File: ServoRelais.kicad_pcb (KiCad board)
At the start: 2 copper layers, 38.7 x 24.9 mm, 20 parts, among them J1 Conn_01x03_Female, J2 ISCP, J3 Conn_01x02_Female, J4 Conn_01x03_Female, U1 L78L05_SOT89, U2 PIC10F320-IP, U3 ASSR-1611

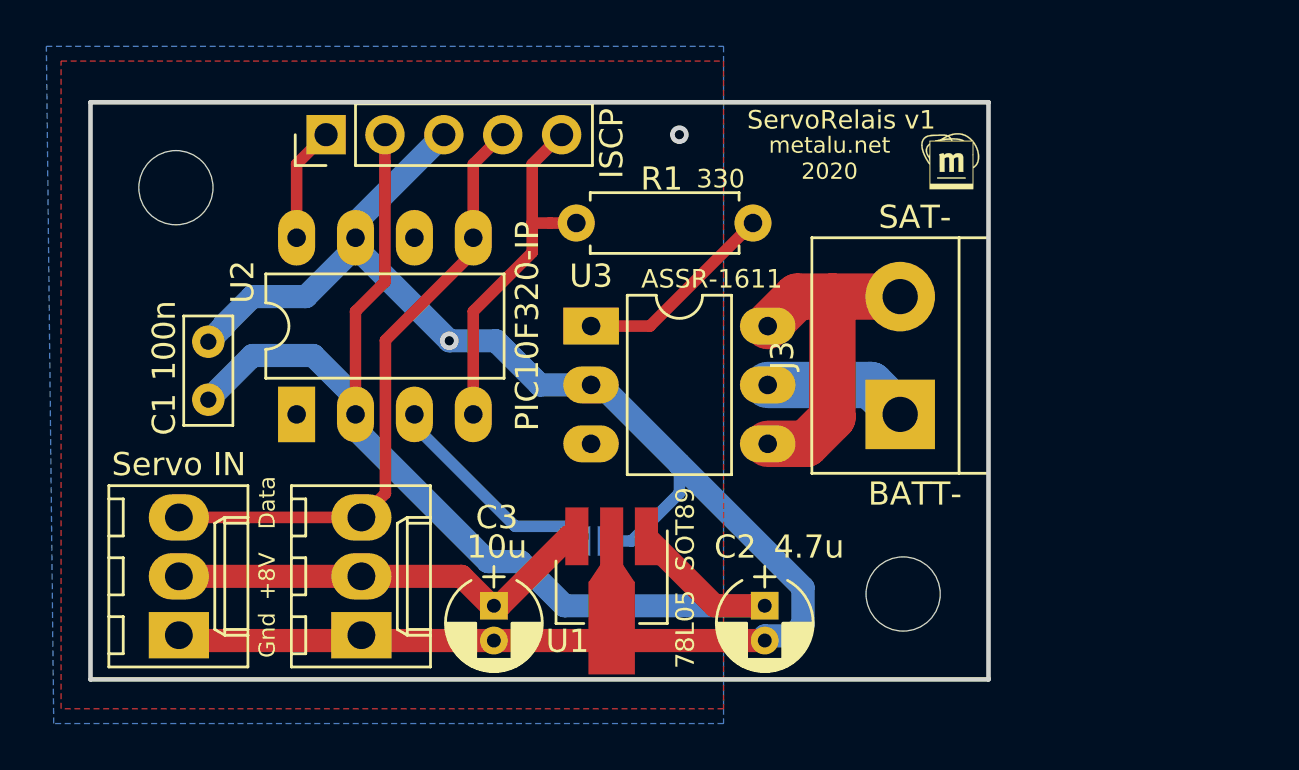
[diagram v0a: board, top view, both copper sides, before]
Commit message: finish PCB, using ASSR-1611 as a 5A circuit breaker.
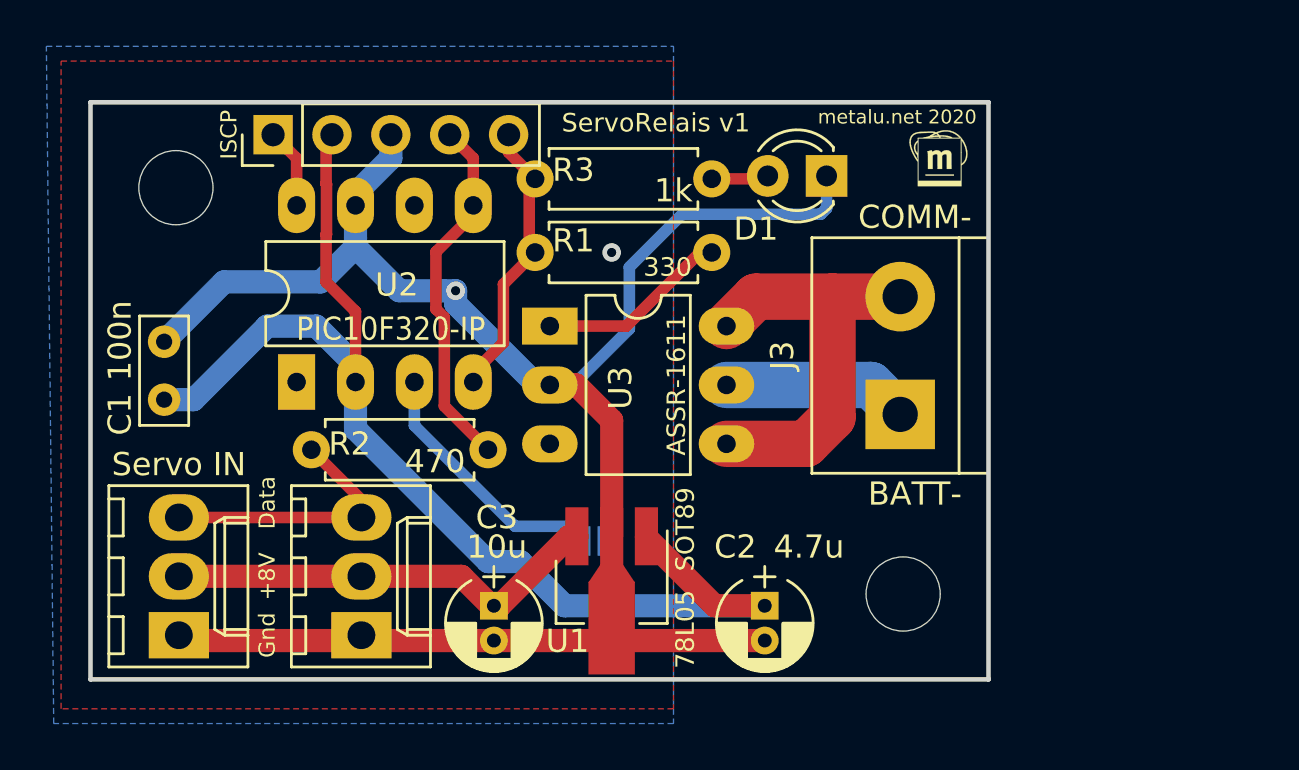
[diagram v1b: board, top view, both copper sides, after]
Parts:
- added D1: LED, LEDs:LED_D3.0mm, F.Cu at (88.4, 33.5)
- added R2: 470, Resistors_ThroughHole:R_Axial_DIN0207_L6.3mm_D2.5mm_P7.62mm_Horizontal, F.Cu at (73.8, 45.3)
- added R3: 1k, Resistors_ThroughHole:R_Axial_DIN0207_L6.3mm_D2.5mm_P7.62mm_Horizontal, F.Cu at (83.4, 33.7)
- moved G*** 15.8 mm to (86.1, 48.1)
- moved J2 2.29 mm to (64.5, 31.8)
- moved R1 2.18 mm to (83.4, 36.8)
- moved C1 1.91 mm to (59.8, 43.2)
- moved U3 1.78 mm to (76.5, 40.0)
- moved U2 1.40 mm to (65.5, 42.4)
- moved G*** 0.52 mm to (93.2, 32.8)
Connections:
- J1 pad 3: /PGD -> Net-(J1-Pad3)
- J4 pad 3: /PGD -> Net-(J1-Pad3)
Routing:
- net Net-(J1-Pad3): track 0.00 -> 11.7 mm
- net /PGD: track 26.9 -> 15.6 mm
- net GND: track 78.5 -> 82.7 mm
- net Net-(J3-Pad2): track 14.7 -> 18.3 mm
- net /PGC: track 15.5 -> 12.0 mm
- net +5V: track 49.0 -> 51.5 mm
- net Net-(D1-Pad2): track 0.00 -> 2.47 mm
- net Net-(J3-Pad1): track 6.24 -> 8.02 mm
- net /Vpp: track 4.97 -> 3.47 mm
- net Net-(JP1-Pad1): track 9.42 -> 10.8 mm
- net Net-(R1-Pad1): track 8.83 -> 8.30 mm
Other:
- board text added: "COMM-"
- board text removed: "SAT-"

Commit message: use a 3v->9V dc-dc converter. version 1.3
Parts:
- removed U3: ASSR-1611, Housings_DIP:DIP-6_W7.62mm_LongPads
- added Q1: IRLB8721PBF, TO_SOT_Packages_SMD:TO-252-2, F.Cu at (83.3, 42.9)
- added Q2: IRLB8721PBF, TO_SOT_Packages_SMD:TO-252-2, F.Cu at (95.1, 45.7)
- added R4: 1k, Resistors_ThroughHole:R_Axial_DIN0207_L6.3mm_D2.5mm_P7.62mm_Horizontal, F.Cu at (97.0, 53.7)
- C3: value 10u -> 100n; footprint Capacitors_ThroughHole:CP_Radial_D4.0mm_P1.50mm -> Capacitors_ThroughHole:C_Rect_L4.6mm_W2.0mm_P2.50mm_MKS02_FKP02
- R1: value 330 -> 1k
- R3: value 1k -> 2.2k
- U1: value L78L05_SOT89 -> MEE1-0309; footprint TO_SOT_Packages_SMD:SOT-89-3_Handsoldering -> Converters_DCDC_ACDC:DCDC-Conv_muRata_CRE1xxxxxxSC
- moved C3 26.3 mm to (94.9, 35.9), turned to 90 degrees
- moved G*** 22.6 mm to (82.0, 52.5)
- moved R3 22.1 mm to (97.0, 51.1)
- moved D1 19.8 mm to (104.5, 45.0), turned to 270 degrees
- moved U1 15.6 mm to (81.9, 35.7), turned to 90 degrees
- moved J3 11.6 mm to (102.4, 39.6)
- moved C2 11.6 mm to (74.2, 52.1)
- moved H2 11.4 mm to (103.1, 51.8)
- moved R1 8.92 mm to (76.2, 42.0), turned to 90 degrees
- moved G*** 5.82 mm to (89.5, 43.4)
- moved C1 3.25 mm to (62.6, 41.5)
- moved JP1 1.35 mm to (79.4, 50.2)
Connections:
- C1 pad 1: +5V -> +3V3
- C2 pad 1: +5V -> +3V3
- C3 pad 1: VCC -> Net-(C3-Pad1)
- C3 pad 2: GND -> GNDPWR
- D1 pad 1: GND -> GNDPWR
- J1 pad 2: VCC -> +3V3
- J2 pad 2: +5V -> +3V3
- J3 pad 1: Net-(J3-Pad1) -> GNDPWR
- J4 pad 2: VCC -> +3V3
- R1 pad 1: Net-(R1-Pad1) -> GND
- R3 pad 2: /PGC -> Net-(C3-Pad1)
- U1 pad 1: +5V -> Net-(Q1-Pad2)
- U1 pad 2: GND -> +3V3
- U1 pad 3: VCC -> GNDPWR
- U2 pad 2: +5V -> +3V3
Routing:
- net +3V3: track 0.00 -> 65.4 mm
- net GNDPWR: track 0.00 -> 58.4 mm
- net +5V: track 51.5 -> 0.00 mm
- net GND: track 82.7 -> 39.8 mm, vias 2 -> 0
- net Net-(C3-Pad1): track 0.00 -> 36.4 mm
- net VCC: track 18.9 -> 0.00 mm
- net Net-(Q1-Pad2): track 0.00 -> 8.69 mm
- net Net-(R1-Pad1): track 8.30 -> 0.00 mm
- net Net-(J3-Pad1): track 8.02 -> 0.00 mm
- net Net-(D1-Pad2): track 2.47 -> 8.97 mm
- net /PGC: track 12.0 -> 17.6 mm
- net Net-(J3-Pad2): track 18.3 -> 13.4 mm
- net Net-(JP1-Pad1): track 10.8 -> 12.4 mm
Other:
- board size 38.7 x 24.9 mm -> 49.9 x 24.9 mm
- board text removed: "78L05"
- board text removed: "SOT89"

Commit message: PCB: add solder-switch to disable powering the DC-DC converter (else programming of the PIC fails because of power loss)
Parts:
- added JP2: (prog), Connect:GS2, B.Cu at (83.1, 39.0)
- moved G*** 3.19 mm to (92.7, 43.2)
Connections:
- U1 pad 2: +3V3 -> Net-(JP2-Pad2)
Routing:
- net Net-(JP2-Pad2): track 0.00 -> 3.62 mm
- net +3V3: track 65.4 -> 61.9 mm
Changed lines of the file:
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@@
     (thickness 1.6)
     (drawings 15)
-    (tracks 98)
+    (tracks 100)
     (zones 0)
-    (modules 25)
-    (nets 13)
+    (modules 26)
+    (nets 14)
   )
   (page User 159.995 110.007)
@@
   (net 11 +3V3)
   (net 12 "Net-(C3-Pad1)")
+  (net 13 "Net-(JP2-Pad2)")
   (net_class Default "This is the default net class."
     (clearance 0.2)
@@
     (add_net "Net-(J3-Pad2)")
     (add_net "Net-(JP1-Pad1)")
+    (add_net "Net-(JP2-Pad2)")
     (add_net "Net-(Q1-Pad2)")
   )
@@
   )
   (module metalunet:metalunet (layer B.Cu)
-    (at 89.535 43.434 180)
+    (at 92.71 43.18 180)
     (fp_text reference G*** (at 3.81 1.143 180) (layer B.SilkS) hide
       (effects (font (size 0.3 0.3) (thickness 0.075)) (justify mirror))
@@
       (net 10 "Net-(Q1-Pad2)"))
     (pad 2 thru_hole oval (at 0 2.54) (size 1.5 2) (drill 0.7) (layers *.Cu *.Mask)
-      (net 11 +3V3))
+      (net 13 "Net-(JP2-Pad2)"))
     (pad 3 thru_hole oval (at 0 5.08) (size 1.5 2) (drill 0.7) (layers *.Cu *.Mask)
       (net 9 GNDPWR))
@@
     )
   )
+  (module Connect:GS2 (layer B.Cu)
+    (at 83.058 38.989 270)
+    (descr "2-pin solder bridge")
+    (tags "solder bridge")
+    (attr smd)
+    (fp_text reference JP2 (at 1.78 0 180) (layer B.SilkS) hide
+      (effects (font (size 1 1) (thickness 0.15)) (justify mirror))
+    )
+    (fp_text value "(prog)" (at 1.524 0 180) (layer B.SilkS)
+      (effects (font (size 0.7 0.7) (thickness 0.1)) (justify mirror))
+    )
+    (fp_line (start -0.89 1.27) (end 0.89 1.27) (layer B.SilkS) (width 0.12))
+    (fp_line (start 0.89 -1.27) (end -0.89 -1.27) (layer B.SilkS) (width 0.12))
+    (fp_line (start 0.89 -1.27) (end 0.89 1.27) (layer B.SilkS) (width 0.12))
+    (fp_line (start -0.89 1.27) (end -0.89 -1.27) (layer B.SilkS) (width 0.12))
+    (fp_line (start -1.1 1.45) (end 1.1 1.45) (layer B.CrtYd) (width 0.05))
+    (fp_line (start -1.1 -1.5) (end -1.1 1.45) (layer B.CrtYd) (width 0.05))
+    (fp_line (start 1.1 -1.5) (end -1.1 -1.5) (layer B.CrtYd) (width 0.05))
+    (fp_line (start 1.1 1.45) (end 1.1 -1.5) (layer B.CrtYd) (width 0.05))
+    (pad 2 smd rect (at 0 -0.64 270) (size 1.27 0.97) (layers B.Cu B.Paste B.Mask)
+      (net 13 "Net-(JP2-Pad2)"))
+    (pad 1 smd rect (at 0 0.64 270) (size 1.27 0.97) (layers B.Cu B.Paste B.Mask)
+      (net 11 +3V3))
+  )
   (dimension 24.892 (width 0.3) (layer F.SilkS)
     (gr_text "24,892 mm" (at 110.712708 42.799 270) (layer F.SilkS)
@@
     (effects (font (size 0.7 0.7) (thickness 0.1)))
   )
-  (gr_text "ServoRelais v1" (at 89.027 40.132) (layer B.SilkS)
+  (gr_text "ServoRelais v1" (at 92.583 40.132) (layer B.SilkS)
     (effects (font (size 0.8 0.8) (thickness 0.15)) (justify mirror))
   )
@@
   (segment (start 81.915 35.687) (end 83.566 37.338) (width 0.5) (layer F.Cu) (net 10))
   (segment (start 83.566 37.338) (end 83.566 41.08) (width 0.5) (layer F.Cu) (net 10))
-  (segment (start 89.408 53.721) (end 89.408 51.054) (width 0.5) (layer F.Cu) (net 12))
-  (segment (start 90.53937 51.054) (end 89.408 51.054) (width 0.5) (layer F.Cu) (net 12))
-  (segment (start 99.323 48) (end 98.05 48) (width 0.5) (layer F.Cu) (net 12))
-  (segment (start 94.996 51.054) (end 90.53937 51.054) (width 0.5) (layer F.Cu) (net 12))
-  (segment (start 98.05 48) (end 94.996 51.054) (width 0.5) (layer F.Cu) (net 12))
-  (segment (start 93.726 46.736) (end 89.408 51.054) (width 0.5) (layer B.Cu) (net 12))
-  (segment (start 93.726 39.878) (end 93.726 46.736) (width 0.5) (layer B.Cu) (net 12))
   (segment (start 66.802 32.004) (end 67.056 31.75) (width 0.5) (layer F.Cu) (net 11))
   (segment (start 66.802 33.860239) (end 66.802 32.004) (width 0.5) (layer F.Cu) (net 11))
@@
   (segment (start 66.379002 40.005) (end 64.262 40.005) (width 1) (layer B.Cu) (net 11))
   (segment (start 64.262 40.005) (end 62.738 41.529) (width 1) (layer B.Cu) (net 11))
-  (segment (start 68.072 42.018) (end 68.072 42.418) (width 0.5) (layer B.Cu) (net 11))
-  (segment (start 83.693 37.973) (end 72.117 37.973) (width 0.5) (layer B.Cu) (net 11))
-  (segment (start 84.455 35.687) (end 84.455 37.211) (width 0.5) (layer B.Cu) (net 11))
-  (segment (start 72.117 37.973) (end 68.072 42.018) (width 0.5) (layer B.Cu) (net 11))
-  (segment (start 84.455 37.211) (end 83.693 37.973) (width 0.5) (layer B.Cu) (net 11))
   (segment (start 60.452 50.8) (end 68.326 50.8) (width 1) (layer F.Cu) (net 11))
   (segment (start 72.898 50.8) (end 74.168 52.07) (width 1) (layer F.Cu) (net 11))
@@
   (segment (start 68.072 44.118) (end 74.168 50.214) (width 0.5) (layer F.Cu) (net 11))
   (segment (start 68.072 42.418) (end 68.072 44.118) (width 0.5) (layer F.Cu) (net 11))
+  (segment (start 72.117 37.973) (end 68.072 42.018) (width 0.5) (layer B.Cu) (net 11))
+  (segment (start 79.629 37.973) (end 72.117 37.973) (width 0.5) (layer B.Cu) (net 11))
+  (segment (start 82.423 38.862) (end 80.518 38.862) (width 0.5) (layer B.Cu) (net 11))
+  (segment (start 68.072 42.018) (end 68.072 42.418) (width 0.5) (layer B.Cu) (net 11))
+  (segment (start 80.518 38.862) (end 79.629 37.973) (width 0.5) (layer B.Cu) (net 11))
+  (segment (start 89.408 53.721) (end 89.408 51.054) (width 0.5) (layer F.Cu) (net 12))
+  (segment (start 90.53937 51.054) (end 89.408 51.054) (width 0.5) (layer F.Cu) (net 12))
+  (segment (start 99.323 48) (end 98.05 48) (width 0.5) (layer F.Cu) (net 12))
+  (segment (start 94.996 51.054) (end 90.53937 51.054) (width 0.5) (layer F.Cu) (net 12))
+  (segment (start 98.05 48) (end 94.996 51.054) (width 0.5) (layer F.Cu) (net 12))
+  (segment (start 93.726 46.736) (end 89.408 51.054) (width 0.5) (layer B.Cu) (net 12))
+  (segment (start 93.726 39.878) (end 93.726 46.736) (width 0.5) (layer B.Cu) (net 12))
   (segment (start 92.456 38.354) (end 94.869 35.941) (width 0.5) (layer B.Cu) (net 12))
   (segment (start 92.202 38.354) (end 93.726 39.878) (width 0.5) (layer B.Cu) (net 12))
   (segment (start 92.202 38.354) (end 92.456 38.354) (width 0.5) (layer B.Cu) (net 12))
   (segment (start 89.535 35.687) (end 92.202 38.354) (width 0.5) (layer B.Cu) (net 12))
+  (segment (start 84.455 38.232) (end 83.698 38.989) (width 0.5) (layer B.Cu) (net 13))
+  (segment (start 84.455 35.687) (end 84.455 38.232) (width 0.5) (layer B.Cu) (net 13))
   (zone (net 1) (net_name GND) (layer F.Cu) (hatch edge 0.508)
     (connect_pads (clearance 0.508))

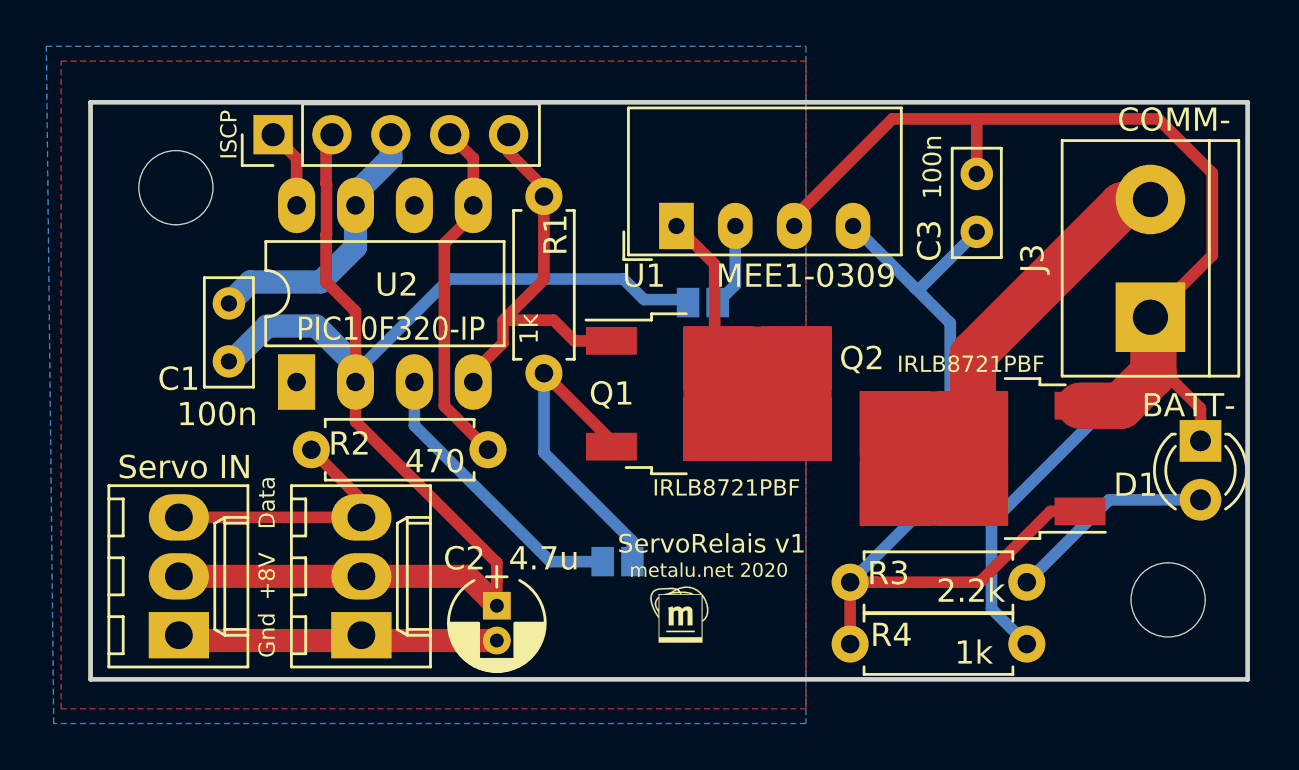
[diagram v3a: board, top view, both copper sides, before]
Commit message: PCB 1.2: add 25Vmax->3V3 regulator
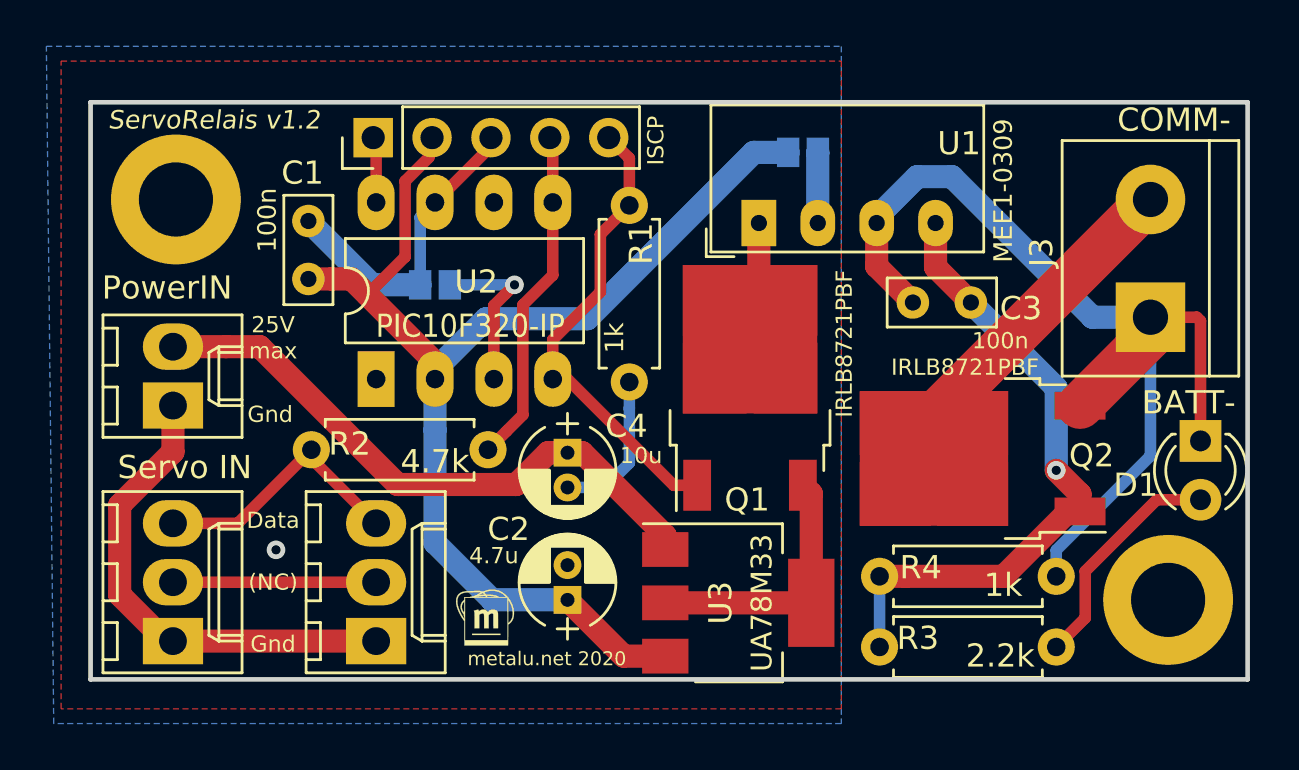
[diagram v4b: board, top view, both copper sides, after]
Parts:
- added C4: 10u, Capacitors_ThroughHole:CP_Radial_D4.0mm_P1.50mm, F.Cu at (77.2, 45.5)
- added J5: PowerIN, Connectors_Molex:Molex_KK-6410-02_02x2.54mm_Straight, F.Cu at (60.2, 43.4)
- added U3: UA78M33, TO_SOT_Packages_SMD:SOT-223-3_TabPin2, F.Cu at (84.6, 51.9)
- H1, H2: footprint Mounting_Holes:MountingHole_3.2mm_M3 -> Mounting_Holes:MountingHole_3.2mm_M3_DIN965_Pad
- J1, J4: value Conn_01x03_Female -> Servo
- J3: value Conn_01x02_Female -> Bornier
- R2: value 470 -> 4.7k
- moved JP1 14.3 mm to (71.5, 38.2), turned to 90 degrees
- moved G*** 8.38 mm to (73.7, 52.6)
- moved JP2 7.78 mm to (87.4, 32.5)
- moved G*** 6.25 mm to (87.8, 47.0)
- moved C1 4.94 mm to (66.0, 38.0)
- moved J2 4.32 mm to (68.8, 31.9)
- moved R1 3.70 mm to (79.9, 42.4)
- moved U1 3.56 mm to (85.5, 35.6)
- moved U2 3.43 mm to (69.0, 42.3)
- moved R4 3.19 mm to (98.3, 50.8)
- moved R3 3.07 mm to (98.3, 53.8)
- moved C3 3.06 mm to (94.6, 39.0), turned to 180 degrees
- moved C2 3.06 mm to (77.2, 51.8), turned to 90 degrees
- moved Q1 1.80 mm to (85.1, 42.7), turned to 90 degrees
- moved J4 0.68 mm to (69.0, 53.6)
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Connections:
- J1 pad 2: +3V3 -> Net-(J1-Pad2)
- J4 pad 2: +3V3 -> Net-(J1-Pad2)
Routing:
- net Net-(C4-Pad1): track 0.00 -> 26.3 mm
- net GNDPWR: track 58.4 -> 44.7 mm
- net GND: track 39.8 -> 52.7 mm, vias 0 -> 1
- net Net-(J1-Pad2): track 0.00 -> 8.76 mm
- net Net-(C3-Pad1): track 36.4 -> 27.9 mm, vias 0 -> 1
- net +3V3: track 61.9 -> 54.1 mm
- net Net-(JP1-Pad1): track 12.4 -> 7.22 mm, vias 0 -> 1
- net Net-(Q1-Pad2): track 8.69 -> 5.17 mm
- net /PGC: track 17.6 -> 20.3 mm
- net Net-(J3-Pad2): track 13.4 -> 15.0 mm
- net Net-(D1-Pad2): track 8.97 -> 10.0 mm
- net /PGD: track 15.3 -> 14.7 mm
- net /Vpp: track 3.47 -> 2.85 mm
- net Net-(JP2-Pad2): track 3.62 -> 3.05 mm
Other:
- board text added: "(NC)"
- board text added: "25V max"
- board text added: "ServoRelais v1.2"
- board text added: "ServoRelais v1.2 metalu.net 2020"
- board text removed: "+8V"
- board text removed: "ServoRelais v1"
